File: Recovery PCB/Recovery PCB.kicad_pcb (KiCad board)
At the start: 4 copper layers, 82.5 x 59 mm, 99 parts, among them J1 Conn_01x02, J10 SMA_GPS, J2 Conn_01x04_Male, J3 MCU Programming Socket, J4 9V_INPUT, J5 Screw_Terminal_01x02, J6 Screw_Terminal_01x02, J7 MEM2075-00-140-01-A, J8 BLD, J9 SMA_LORA, K1 SANYOU_SRD_Form_C, K2 SANYOU_SRD_Form_C, Q1 BSS138, Q2 BSS138, Q3 BSS138, SW1 SW_SPDT, SW2 SW_Push, U1 MIC5528-3.3YMT-TR, U2 ATSAMD21G18A-AUT, U3 MS5607-02BA, U4 ADXL377, U5 BNO055, U6 RFM95W-915S2, U7 CAM-M8, Y1 32.768kHz, Y2 32.768k

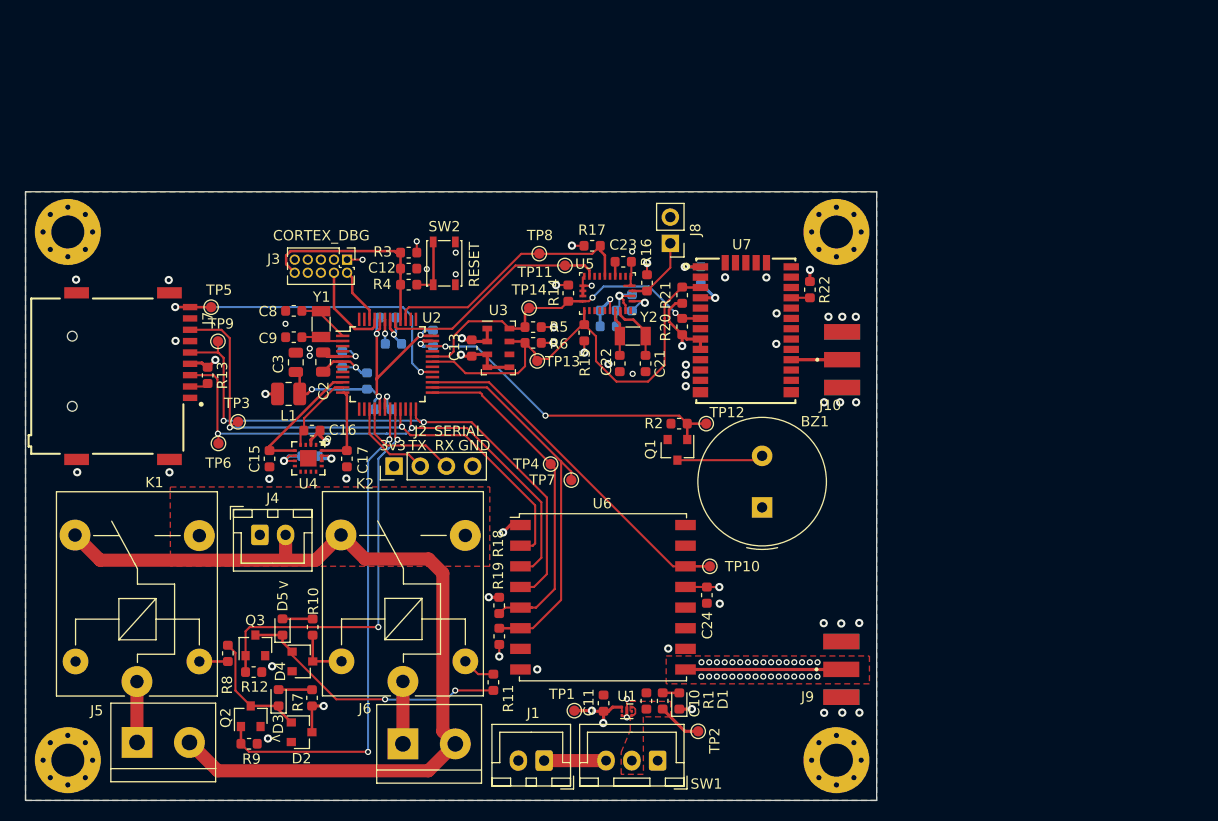
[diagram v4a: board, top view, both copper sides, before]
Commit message: Recovery PCB: Tweak Motion Axes
Reconciled IMU and accelerometer motion axes and added models for edge
connectors.
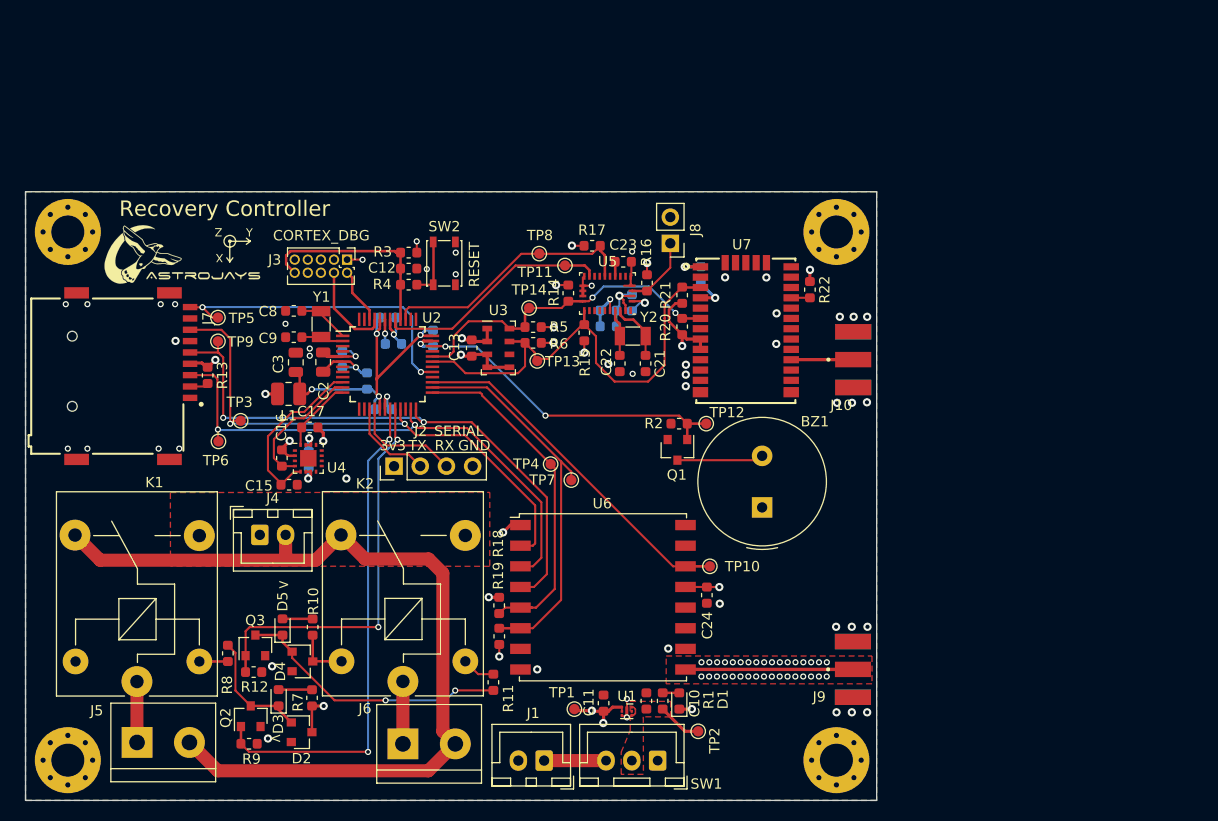
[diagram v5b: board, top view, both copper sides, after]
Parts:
- added ?: , , F.Cu at (115.2, 91.7)
- added ?: , , F.Cu at (113.0, 71.0)
- added G***: LOGO, AJ_GFX:full_logo_21.3mmx9.3mm, F.Cu at (109.3, 72.3)
- U5: footprint Package_LGA:LGA-28_5.2x3.8mm_P0.5mm -> Parts:LGA-28_5.2x3.8mm_P0.5mm
- moved C17 4.70 mm to (120.0, 89.3), turned to 0 degrees
- moved C16 3.95 mm to (117.3, 92.3), turned to 90 degrees
- moved C15 3.16 mm to (118.0, 94.9), turned to 0 degrees
- moved TP5 1.21 mm to (111.2, 78.7)
- moved J9 1.13 mm to (172.7, 112.8)
- moved J10 1.08 mm to (172.7, 82.8)
- moved C14 0.34 mm to (120.0, 92.5), turned to 270 degrees
- moved TP3 0.27 mm to (113.3, 88.7)
- moved TP6 0.20 mm to (111.2, 90.7)
- moved TP1 0.15 mm to (145.7, 116.7)
- turned U4 to 0 degrees
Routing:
- net /Yout: track 7.70 -> 12.9 mm
- net /Xout: track 12.5 -> 17.1 mm
- net /SD_CS: track 33.7 -> 30.7 mm
- net /radio-915-lora/LoRa_RF: track 15.1 -> 16.2 mm
- net /Zout: track 8.32 -> 7.18 mm
- net /gps-module/GPS_RF: track 4.94 -> 6.02 mm
- net GND: track 50.9 -> 50.1 mm, vias 87 -> 93
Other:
- board text added: "Recovery Controller"
- board text added: "X"
- board text added: "Y"
- board text added: "Z"

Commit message: Recovery PCB: Fix relay
Replaced unavailable relay with a correct part and replaced voltage
regulator with an easier to solder alternative.
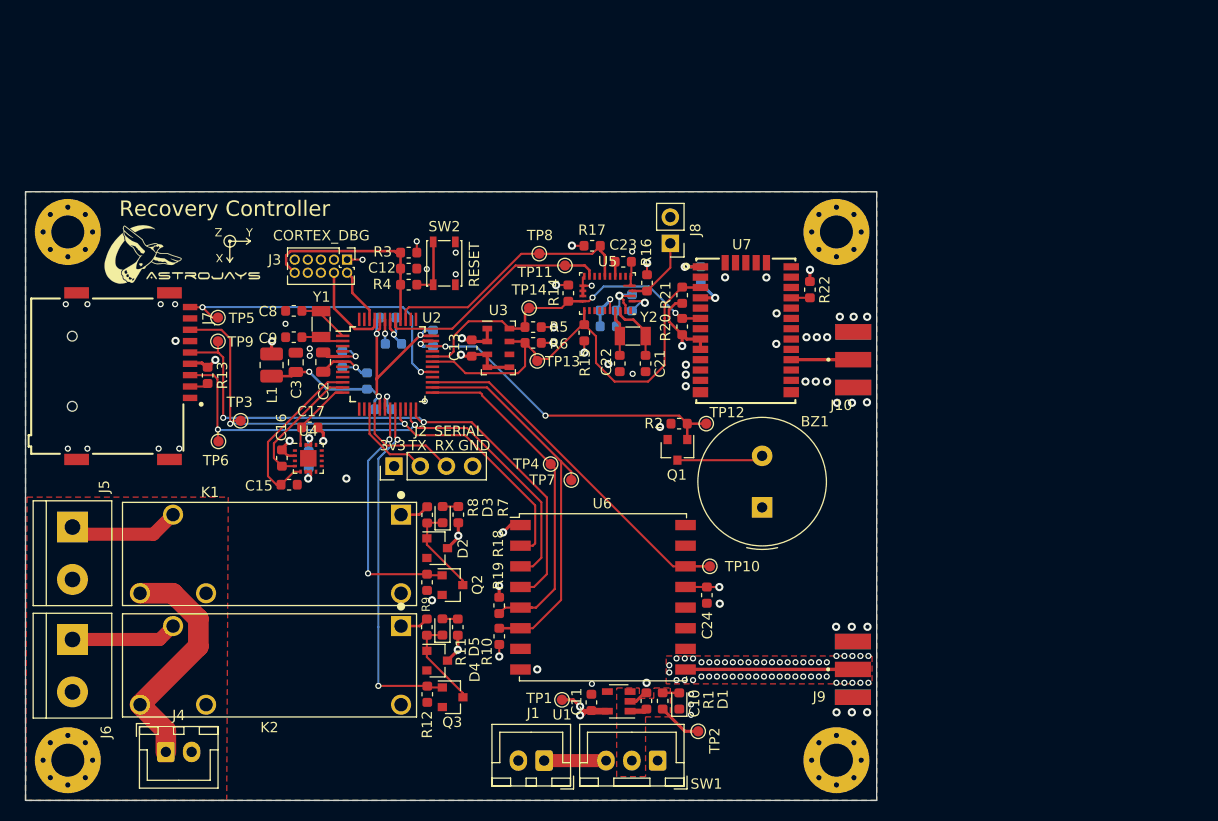
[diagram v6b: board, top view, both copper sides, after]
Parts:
- C10, C11: value 2.2u -> 1u
- K1, K2: value SANYOU_SRD_Form_C -> G6RL-14-ASI-DC3; footprint Relay_THT:Relay_SPDT_SANYOU_SRD_Series_Form_C -> Parts:RELAY_G6RL-1
- R11, R8: value 300 -> 5
- U1: value MIC5528-3.3YMT-TR -> AP7366-33W5-7; footprint Package_DFN_QFN:DFN-6-1EP_1.2x1.2mm_P0.4mm_EP0.3x0.94mm_PullBack -> Package_TO_SOT_SMD:SOT-23-5
- moved J6 33.6 mm to (97.0, 109.9), turned to 270 degrees
- moved K1 30.3 mm to (128.9, 97.8), turned to 180 degrees
- moved D3 23.8 mm to (132.9, 97.8)
- moved R8 23.5 mm to (131.4, 97.8), turned to 270 degrees
- moved Q2 23.3 mm to (133.9, 104.6), turned to 0 degrees
- moved R9 23.3 mm to (131.4, 104.4), turned to 270 degrees
- moved J4 22.9 mm to (106.1, 120.8)
- moved R7 22.7 mm to (134.4, 97.8)
- moved D2 22.2 mm to (132.4, 101.0)
- moved J5 21.8 mm to (97.0, 99.0), turned to 270 degrees
- moved Q3 19.8 mm to (133.9, 115.5), turned to 0 degrees
- moved R12 17.0 mm to (131.4, 115.2), turned to 270 degrees
- moved D5 15.5 mm to (132.9, 108.7)
- moved R10 14.1 mm to (134.4, 108.7)
- moved D4 13.1 mm to (132.4, 112.0)
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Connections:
- K1 pad 1: Net-(J5-Pad1) -> Net-(K1-Pad1)
- K1 pad 2: Net-(K1-Pad2) -> Net-(J5-Pad1)
- K2 pad 1: Net-(J6-Pad1) -> Net-(K2-Pad1)
- K2 pad 2: Net-(K2-Pad2) -> Net-(J6-Pad1)
- R11 pad 1: Net-(K2-Pad2) -> Net-(K2-Pad1)
- R8 pad 1: Net-(K1-Pad2) -> Net-(K1-Pad1)
- U1 pad 1: +3V3 -> +BATT
- U1 pad 2: +3V3 -> GND
- U1 pad 3: GND -> +BATT
- U1 pad 4: +BATT -> Net-(U1-Pad4)
- U1 pad 5: Net-(U1-Pad5) -> +3V3
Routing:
- net GNDPWR: track 86.8 -> 0.00 mm
- net /IN1: track 48.4 -> 24.1 mm
- net +9V: track 0.00 -> 23.0 mm
- net Net-(D4-Pad2): track 26.8 -> 8.98 mm, vias 2 -> 0
- net /IN2: track 39.0 -> 34.0 mm
- net Net-(J5-Pad1): track 5.90 -> 10.3 mm
- net Net-(J6-Pad1): track 6.05 -> 10.3 mm
- net Net-(K2-Pad2): track 3.24 -> 0.00 mm
- net Net-(K1-Pad1): track 0.00 -> 2.85 mm
- net Net-(K2-Pad1): track 0.00 -> 2.78 mm
- net Net-(K1-Pad2): track 2.76 -> 0.00 mm
- net Net-(D2-Pad2): track 11.6 -> 8.99 mm
- net +3V3: track 60.9 -> 58.3 mm, vias 22 -> 23
- net GND: track 50.1 -> 47.6 mm, vias 93 -> 119
- net Net-(D3-Pad2): track 3.24 -> 1.52 mm
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- added copper zone on F.Cu, net GNDPWR
- removed copper zone on F.Cu, net +9V
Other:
- board text removed: "<"
- board text removed: ">"

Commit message: Recovery PCB: Add coplanar wave guide for GPS RF trace.
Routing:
- net GND: vias 119 -> 133
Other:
- net class RF 50 Ohm: trace_width 0.319024 -> 0.325628
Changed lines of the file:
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@@
-(kicad_pcb (version 20171130) (host pcbnew 5.1.9)
+(kicad_pcb (version 20171130) (host pcbnew "(5.1.4)-1")
   (general
     (thickness 1.6)
     (drawings 25)
-    (tracks 671)
+    (tracks 685)
     (zones 0)
     (modules 102)
@@
     (user_trace_width 2)
     (trace_clearance 0.2)
-    (zone_clearance 0.35)
+    (zone_clearance 0.2)
     (zone_45_only no)
     (trace_min 0.13)
@@
   (net_class "RF 50 Ohm" ""
     (clearance 0.2)
-    (trace_width 0.319024)
+    (trace_width 0.325628)
     (via_dia 0.6)
     (via_drill 0.35)
@@
   (gr_line (start 175 125.5) (end 92.5 125.5) (layer Edge.Cuts) (width 0.05))
   (gr_line (start 175 66.5) (end 175 125.5) (layer Edge.Cuts) (width 0.05))
-  (via (at 156.4 111.74) (size 0.6) (drill 0.35) (layers F.Cu B.Cu) (net 3))
-  (via (at 155.6 111.74) (size 0.6) (drill 0.35) (layers F.Cu B.Cu) (net 3))
-  (via (at 157.2 111.74) (size 0.6) (drill 0.35) (layers F.Cu B.Cu) (net 3))
   (segment (start 163.48 92.52) (end 163.9 92.1) (width 0.2032) (layer F.Cu) (net 1))
   (segment (start 155.69 92.52) (end 163.48 92.52) (width 0.2032) (layer F.Cu) (net 1))
@@
   (segment (start 147.4125 116.85) (end 147.35 116.7875) (width 0.508) (layer F.Cu) (net 2))
   (segment (start 148.9 116.85) (end 147.4125 116.85) (width 0.65) (layer F.Cu) (net 2))
+  (via (at 156.4 111.74) (size 0.6) (drill 0.35) (layers F.Cu B.Cu) (net 3))
+  (via (at 155.6 111.74) (size 0.6) (drill 0.35) (layers F.Cu B.Cu) (net 3))
+  (via (at 157.2 111.74) (size 0.6) (drill 0.35) (layers F.Cu B.Cu) (net 3))
   (via (at 107 77.4) (size 0.6) (drill 0.35) (layers F.Cu B.Cu) (net 3))
   (via (at 170.17 112.11) (size 0.6) (drill 0.35) (layers F.Cu B.Cu) (net 3))
@@
   (via (at 152.7 114.1) (size 0.8) (drill 0.4) (layers F.Cu B.Cu) (net 3))
   (via (at 154 89.3) (size 0.8) (drill 0.4) (layers F.Cu B.Cu) (net 3))
-  (via (at 168.1 84.9) (size 0.8) (drill 0.4) (layers F.Cu B.Cu) (net 3))
-  (via (at 169.1 84.9) (size 0.8) (drill 0.4) (layers F.Cu B.Cu) (net 3))
-  (via (at 170.2 84.9) (size 0.8) (drill 0.4) (layers F.Cu B.Cu) (net 3))
-  (via (at 168.2 80.6) (size 0.8) (drill 0.4) (layers F.Cu B.Cu) (net 3))
-  (via (at 169.2 80.6) (size 0.8) (drill 0.4) (layers F.Cu B.Cu) (net 3))
-  (via (at 170.2 80.6) (size 0.8) (drill 0.4) (layers F.Cu B.Cu) (net 3))
   (via (at 157 117.2) (size 0.6) (drill 0.35) (layers F.Cu B.Cu) (net 3))
   (via (at 157 116.2) (size 0.6) (drill 0.35) (layers F.Cu B.Cu) (net 3))
@@
   (via (at 154.9 113.1) (size 0.6) (drill 0.35) (layers F.Cu B.Cu) (net 3))
   (via (at 131.2 86.8) (size 0.6) (drill 0.35) (layers F.Cu B.Cu) (net 3))
+  (via (at 168 82.1) (size 0.6) (drill 0.35) (layers F.Cu B.Cu) (net 3))
+  (via (at 168.7 82.1) (size 0.6) (drill 0.35) (layers F.Cu B.Cu) (net 3))
+  (via (at 169.4 82.1) (size 0.6) (drill 0.35) (layers F.Cu B.Cu) (net 3))
+  (via (at 170.1 82.1) (size 0.6) (drill 0.35) (layers F.Cu B.Cu) (net 3))
+  (via (at 165.25 82.47) (size 0.6) (drill 0.35) (layers F.Cu B.Cu) (net 3))
+  (via (at 165.25 83.08) (size 0.6) (drill 0.35) (layers F.Cu B.Cu) (net 3))
+  (via (at 168 83.5) (size 0.6) (drill 0.35) (layers F.Cu B.Cu) (net 3))
+  (via (at 168.7 83.5) (size 0.6) (drill 0.35) (layers F.Cu B.Cu) (net 3))
+  (via (at 169.4 83.5) (size 0.6) (drill 0.35) (layers F.Cu B.Cu) (net 3))
+  (via (at 170.1 83.5) (size 0.6) (drill 0.35) (layers F.Cu B.Cu) (net 3))
+  (via (at 171.1 81.5) (size 0.6) (drill 0.35) (layers F.Cu B.Cu) (net 3))
+  (via (at 171.8 81.5) (size 0.6) (drill 0.35) (layers F.Cu B.Cu) (net 3))
+  (via (at 172.5 81.5) (size 0.6) (drill 0.35) (layers F.Cu B.Cu) (net 3))
+  (via (at 173.2 81.5) (size 0.6) (drill 0.35) (layers F.Cu B.Cu) (net 3))
+  (via (at 173.9 81.5) (size 0.6) (drill 0.35) (layers F.Cu B.Cu) (net 3))
+  (via (at 171.1 84.1) (size 0.6) (drill 0.35) (layers F.Cu B.Cu) (net 3))
+  (via (at 171.8 84.1) (size 0.6) (drill 0.35) (layers F.Cu B.Cu) (net 3))
+  (via (at 172.5 84.1) (size 0.6) (drill 0.35) (layers F.Cu B.Cu) (net 3))
+  (via (at 173.2 84.1) (size 0.6) (drill 0.35) (layers F.Cu B.Cu) (net 3))
+  (via (at 173.9 84.1) (size 0.6) (drill 0.35) (layers F.Cu B.Cu) (net 3))
   (segment (start 126.841569 87.57) (end 126.841569 86.42797) (width 0.254) (layer F.Cu) (net 4) (status 10))
   (segment (start 126.841569 86.42797) (end 126.750102 86.336503) (width 0.254) (layer F.Cu) (net 4))
@@
   (segment (start 166.721569 82.78) (end 166.72 82.781569) (width 0.319024) (layer F.Cu) (net 37))
   (segment (start 166.726569 82.775) (end 166.72 82.781569) (width 0.319024) (layer F.Cu) (net 37))
-  (segment (start 172.725 82.775) (end 166.726569 82.775) (width 0.319024) (layer F.Cu) (net 37))
+  (segment (start 172.725 82.775) (end 166.726569 82.775) (width 0.313115) (layer F.Cu) (net 37))
   (segment (start 130.76 93.1) (end 129.608399 91.948399) (width 0.2032) (layer F.Cu) (net 38))
   (segment (start 129.608399 91.948399) (end 127.809124 91.948399) (width 0.2032) (layer F.Cu) (net 38))
@@
     )
   )
-  (zone (net 0) (net_name "") (layer F.Cu) (hatch edge 0.508)
-    (connect_pads thru_hole_only (clearance 0.16))
-    (min_thickness 0.14)
-    (keepout (tracks allowed) (vias allowed) (copperpour not_allowed))
-    (fill (arc_segments 32) (thermal_gap 0.508) (thermal_bridge_width 0.508))
-    (polygon
-      (pts
-        (xy 175.05 84.45) (xy 167.48 84.46) (xy 167.48 81.06) (xy 175.05 81.05)
-      )
-    )
-  )
   (zone (net 3) (net_name GND) (layer F.Cu) (hatch edge 0.508)
     (connect_pads thru_hole_only (clearance 0.2))
@@
       )
     )
+  )
+  (zone (net 3) (net_name GND) (layer F.Cu) (hatch edge 0.508)
+    (connect_pads thru_hole_only (clearance 0.2))
+    (min_thickness 0.1)
+    (fill yes (arc_segments 32) (thermal_gap 0.508) (thermal_bridge_width 0.508))
+    (polygon
+      (pts
+        (xy 174.57 81.6) (xy 165.7 81.6) (xy 165.7 84) (xy 174.57 84)
+      )
+    )

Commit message: Recovery PCB: Deleted excess pullup resistors, redid mounting holes.
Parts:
- removed ? (x2): , 
- removed G***: LOGO, AJ_GFX:full_logo_21.3mmx9.3mm
- removed R14, R15: 4.7k, Resistor_SMD:R_0603_1608Metric
- removed R20, R21: 2.2k, Resistor_SMD:R_0603_1608Metric
- removed REF** (x4): MountingHole_3.2mm_M3_Pad_Via, MountingHole:MountingHole_3.2mm_M3_Pad_Via
- added H1: MountingHole, MountingHole:MountingHole_3.2mm_M3_Pad_Via, F.Cu at (96.6, 70.5)
- added H2: MountingHole, MountingHole:MountingHole_3.2mm_M3_Pad_Via, F.Cu at (171.0, 70.5)
- added H3: MountingHole, MountingHole:MountingHole_3.2mm_M3_Pad_Via, F.Cu at (96.6, 121.5)
- added H4: MountingHole, MountingHole:MountingHole_3.2mm_M3_Pad_Via, F.Cu at (171.0, 121.5)
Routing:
- net +3V3: track 58.3 -> 49.9 mm, vias 23 -> 21
